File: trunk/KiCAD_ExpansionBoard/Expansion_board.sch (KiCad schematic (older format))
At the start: 2 parts

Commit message: Creation of project (sheets) structure and add some library schematic component (transceiver.lib, headers, etc.)
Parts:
- removed IC?: PIC16F876P, microchip-DIL28-6, symbol PIC16F876P
- removed P?: CONN_11, symbol CONN_11
- added U?: SN65HVD11, MODULE, symbol SN65HVD11
- added U?: SN65HVD234, MODULE, symbol SN65HVD234
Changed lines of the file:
@@
 EESchema Schematic File Version 2
+LIBS:boosterpack
 LIBS:power
 LIBS:device
@@
 LIBS:contrib
 LIBS:valves
+LIBS:transceiver
 LIBS:TM4C123G_CommExpBoard-cache
 EELAYER 27 0
@@
 Date "9 jun 2014"
 Rev "0.1"
-Comp "Luca Buccolini, student @ Università Politecnica delle Marche"
+Comp "Luca Buccolini, Student @ Università Politecnica delle Marche"
 Comment1 "Expansion Board for the Texas Instruments TM4C123G Launchpad "
 Comment2 ""
@@
 $EndDescr
 $Comp
-L PIC16F876P IC?
-U 1 1 5395B88F
-P 5150 2650
-F 0 "IC?" H 4450 3600 50  0000 L BNN
-F 1 "PIC16F876P" H 5450 1650 50  0000 L BNN
-F 2 "microchip-DIL28-6" H 5150 2800 50  0001 C CNN
-F 3 "" H 5150 2650 60  0000 C CNN
-	1    5150 2650
+L SN65HVD11 U?
+U 1 1 5395F741
+P 5350 2200
+F 0 "U?" H 5350 2100 50  0000 C CNN
+F 1 "SN65HVD11" H 5350 2300 50  0000 C CNN
+F 2 "MODULE" H 5350 2200 50  0001 C CNN
+F 3 "http://www.farnell.com/datasheets/1808277.pdf" H 5350 2200 50  0001 C CNN
+F 4 "Farnell" H 5350 2200 50  0001 C CNN "Supplier 1"
+F 5 "1100955" H 5350 2200 50  0001 C CNN "Supplier 1 P/N"
+F 6 "SN65HVD11D" H 5350 2200 50  0001 C CNN "Producer P/N"
+	1    5350 2200
 	1    0    0    -1
 $EndComp
 $Comp
-L CONN_11 P?
-U 1 1 5395B89E
-P 8250 3350
-F 0 "P?" V 8200 3350 60  0000 C CNN
-F 1 "CONN_11" V 8300 3350 60  0000 C CNN
-F 2 "" H 8250 3350 60  0000 C CNN
-F 3 "" H 8250 3350 60  0000 C CNN
-	1    8250 3350
+L SN65HVD234 U?
+U 1 1 5395F75E
+P 8250 2250
+F 0 "U?" H 8250 2150 50  0000 C CNN
+F 1 "SN65HVD234" H 8250 2350 50  0000 C CNN
+F 2 "MODULE" H 8250 2250 50  0001 C CNN
+F 3 "http://www.farnell.com/datasheets/1808424.pdf" H 8250 2250 50  0001 C CNN
+F 4 "Farnell" H 8250 2250 50  0001 C CNN "Supplier 1"
+F 5 "1212363" H 8250 2250 50  0001 C CNN "Supplier 1 P/N"
+F 6 "SN65HVD234D" H 8250 2250 50  0001 C CNN "Producer P/N"
+	1    8250 2250
 	1    0    0    -1
 $EndComp

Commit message: Circuit board schematic complete! TODO: Update schematic according new received specifics: "note-expansionboard_20140623.txt"
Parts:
- added C1: 10u, ~, symbol C
- added C2, C4: 100n, ~, symbol C
- added C3: 22u, ~, symbol C
- added D1: LED_R, SM_0603_MD, symbol LED
- added L1: 2u2, ~, symbol INDUCTOR_SMALL
- added P5: ANT, ~, symbol TST
- added Q1: NTR4101P, ~, symbol MOS_P
- added R1, R10, R11, R16, R17: 0, ~, symbol R
- added R12: 750, ~, symbol R
- added R13, R15: 560, ~, symbol R
- added R14, R4: 120, ~, symbol R
- added R18, R2, R7, R8, R9: 10k, ~, symbol R
- added R3: 100k, ~, symbol R
- added R5: 300k, ~, symbol R
- added R6: 95k3, ~, symbol R
- added SW? (x3): DIP_SWITCH, ~, symbol DIP_SWITCH
- added SW?: DIP_SWITCH_X1, ~, symbol DIP_SWITCH_X1
- added TVS1, TVS2: CDSOT23-SM712, ~, symbol CDSOT23-SM712
- added U2: TPS62160, MODULE, symbol TPS62160
- added U4: RFM23B, symbol RFM23B
- U1: renamed from U?; Descriprion (none) -> TRANSCEIVER CAN, 65HVD234, SOIC8; Producer (none) -> Texas Instruments
- U3: renamed from U?; Descriprion (none) -> 3.3-V RS-485 TRANSCEIVERS; Producer (none) -> Texas Instruments
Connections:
- net labels added: +12V_BUS, +3.3V_EB, +3.3V_TLP, +5V_TLP, CAN0_EN, CAN0_RS, CAN0_RX, CAN0_TX, CAN_H, CAN_L, GND, RFM_CLK, RFM_GPIO0, RFM_GPIO1, RFM_MISO, RFM_MOSI, RFM_NIRQ, RFM_SCLK, RFM_SDN, RFM_SSEL, RS485_A, RS485_B, RS485_RXEN#, RS485_TXEN, UART3_RX, UART3_TX
- wire segments 0 -> 126
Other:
- note added: "CAN transceiver"
- note added: "Power supply\n"
- note added: "RF module"
- note added: "RS-485 transceiver"
- note added: "Resistor on CAN0_RS line is \nfor slope control (optional)"
- note added: "mount R 10 ohm in place \nof R 0 ohm to improve \nsurge/ESD/EFT protection"
- moved on the sheet: U1, U3

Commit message: -Unito le due linee a 3.3V e riposizionato Q1 che ora va ad interrompere la linea di alimentazione a 3.3V dello switching quando è presente la +5V_TLP (USB). In serie al gate ho messo R8 da 120 ohm e ho lasciato R7 da 10k di pull-down.
-Ho messo un NPN, Q3, che ha al suo interno un partitore da 22k + 47k; è pilotato dalla +5V_TLP ed ho messo R1 verso +12V_BUS che mantiene attivo lo switching a meno che non sia presente la +5V_TLP (Q3 ON). Infine ho posizionato il led a monte del PMOS.

-Per la protezione dalle sovratensioni sulla +5V_TLP ho inserito, all'ingesso, TVS4 che è bidirezionale con tensione di lavoro a 5V e tensione di breakdown di 5.8V (min).

-Rimosse tutte le resistenze di pull-up nei transceiver: ne avevano alcune già internamente.

-Sostituiti gli header-jumper per i terminatori e la rete di fail-safe biasing con un SPDT (SW1), ed un 4PDT (SW2).

In serie al pin RS del transceiver ho messo una 10k.

Pull-up da 10k su SDN dell'RF module
 
Ho inserito un secondo TP P1, ANT_GND che posizionerò vicino al primo, P5, ANT_C per il collegamento dell'antenna.

-MISURA DELLA TENSIONE DI BUS: V_AN_MONITOR: ho ricalcolato i valori di R19 e R20 per ottenere un divider ratio pari a 6.236 circa anziché 6.206 come indicato. La tensione di fondo scala sarà vicina ai 20 V.

-Il TVS3 (SMCJ12CA) indicato è bidirezionale (DS: http://www.farnell.com/datasheets/1794554.pdf), così ho corretto il simbolo mettendone uno appropriato.

-Sostituito lo "spare-function header" da 2x4 pin con uno 2x5 pin reimpostando pin-out come indicato, comprensivo di massa ed alimentazione.
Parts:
- removed R9: 10k, ~, symbol R
- removed SW? (x3): DIP_SWITCH, ~, symbol DIP_SWITCH
- removed SW?: DIP_SWITCH_X1, ~, symbol DIP_SWITCH_X1
- added P1: ANT_GND, ~, symbol TST
- added Q3: PDTC124XT, SOT23_MD, symbol NPN_DIGITAL
- added SW1: SLIDE_SWITCH_SPDT, ~, symbol SLIDE_SWITCH_SPDT
- added SW2: SLIDE_SWITCH_4PDT, ~, symbol SLIDE_SWITCH_4PDT
- P5: value ANT -> ANT_C
- R1: value 0 -> 10k; Descriprion RESISTORE, 0805, 0R, ANTI SOLFATAZIONE -> RESISTOR, 0805, 10K, 1%, ANTI SULFUR; Producer P/N MCMR08X000 PTL -> MCMR08X1002FTL; Supplier 1 P/N 2073603 -> 2073607
- R8: value 10k -> 120; Descriprion RESISTOR, 0805, 10K, 1%, ANTI SULFUR -> RESISTOR, 0805, 120R, 1%, ANTI SULFUR; Producer P/N MCMR08X1002FTL -> MCMR08X1200FTL; Supplier 1 P/N 2073607 -> 2073624
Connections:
- net labels added: +3.3V
- net labels removed: +3.3V_EB, +3.3V_TLP
- wire segments 126 -> 128
- no-connect marks 0 -> 4
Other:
- note removed: "Resistor on CAN0_RS line is \nfor slope control (optional)"
- moved on the sheet: C1, C2, C3, C4, D1, L1, P5, Q1, R10, R11, R12, R13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

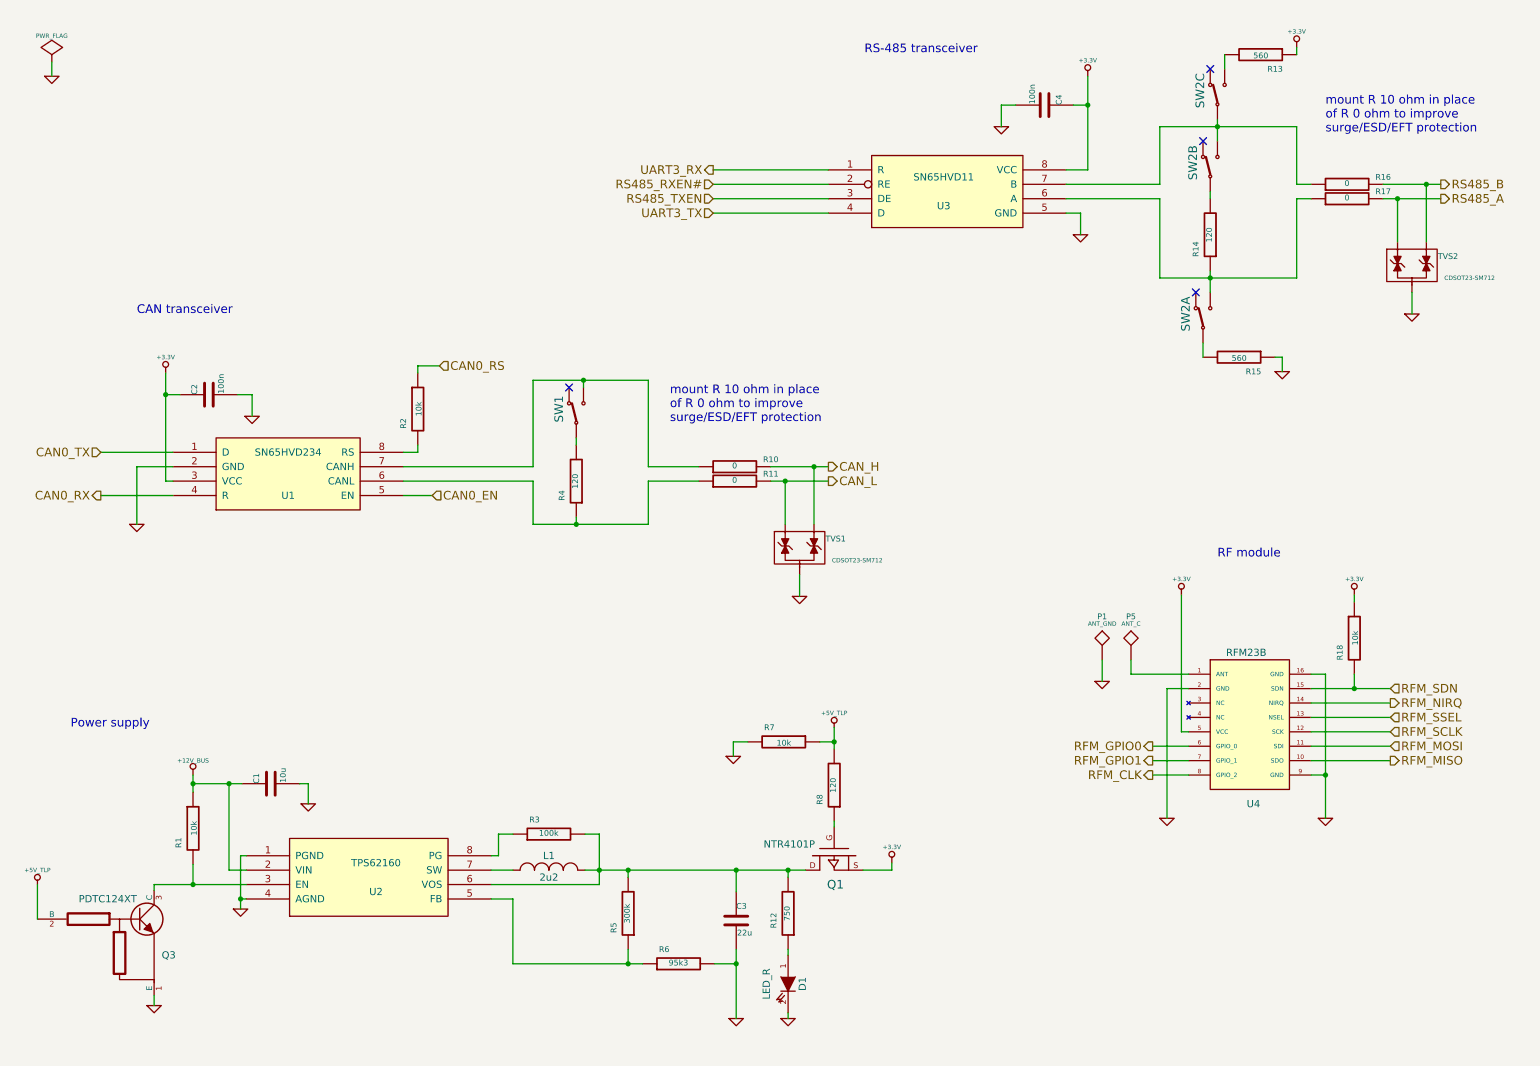
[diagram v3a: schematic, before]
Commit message: -Eliminata R7> con l-aggiunta di Q3 ora il pull down [ incorporato in esso, un-altro sprecher' solo corrente -Aumentate R1 e R18 a 100k -Modificata la connessione di SW2 per minimizzare la capacit' sul bus
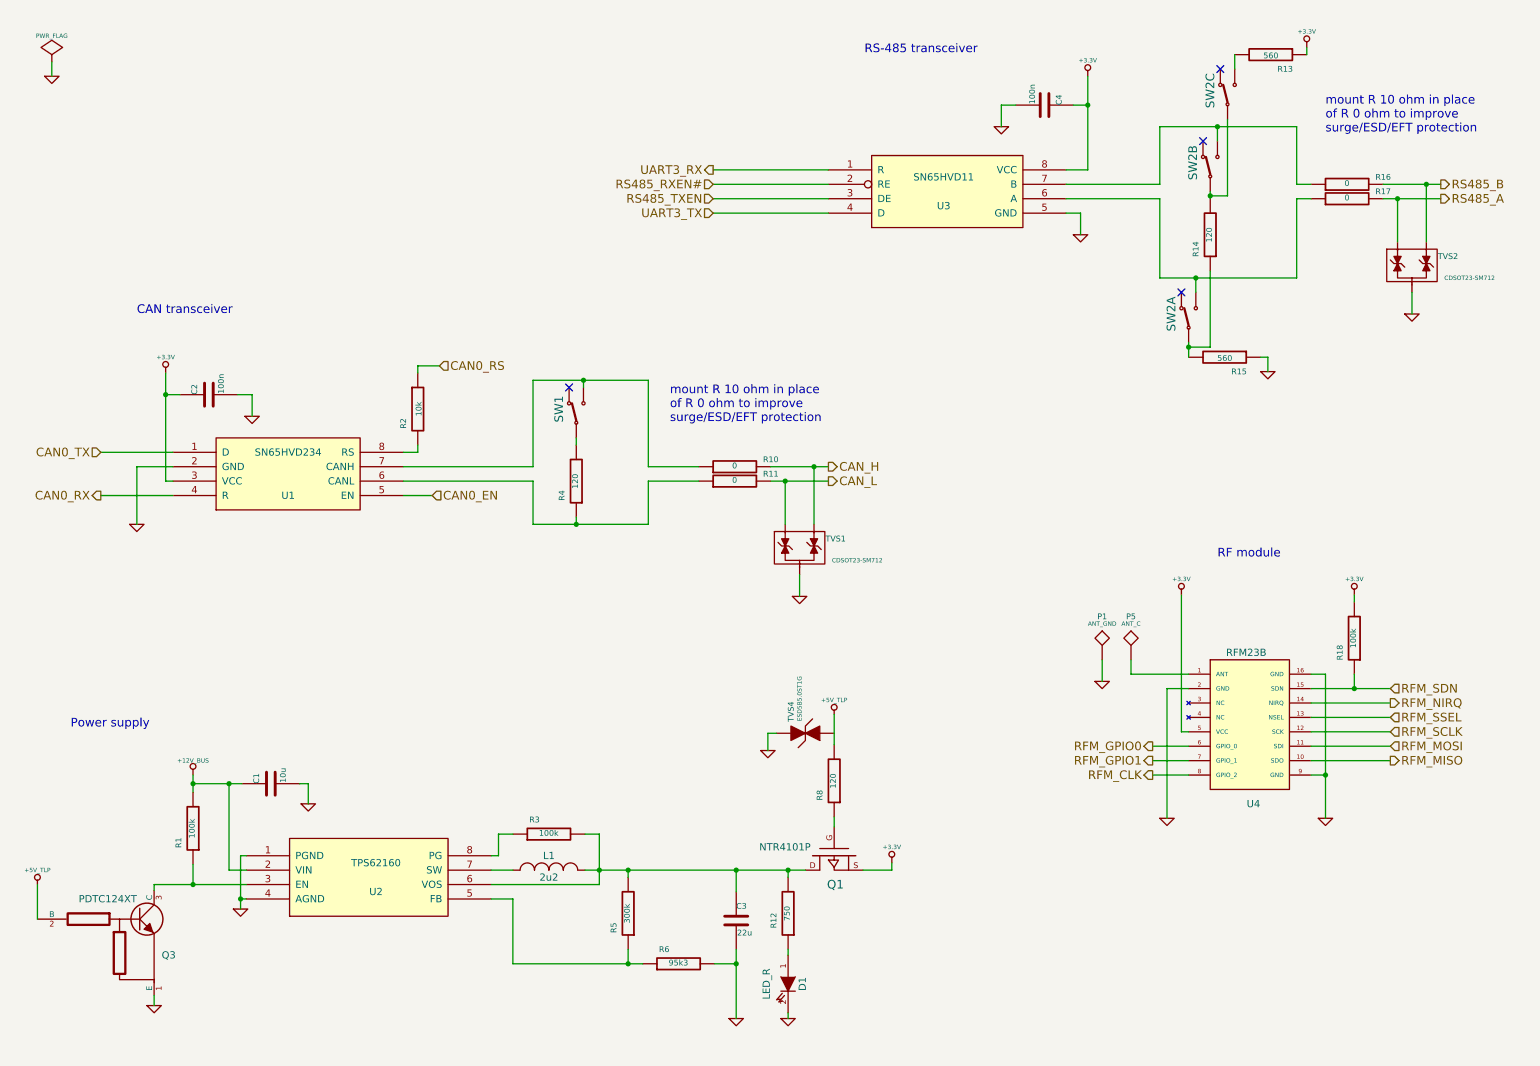
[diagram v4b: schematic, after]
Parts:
- removed R7: 10k, ~, symbol R
- added TVS4: ESD5B5.0ST1G, SOD-523_MD, symbol BID_TVS
- R1, R18: value 10k -> 100k; Descriprion RESISTOR, 0805, 10K, 1%, ANTI SULFUR -> RESISTOR, 0805, 100K, 1%, THICK FILM CHIP RESISTOR; Producer MULTICOMP -> VISHAY DRALORIC; Producer P/N MCMR08X1002FTL -> CRCW0805100KFKTA; Supplier 1 P/N 2073607 -> 1652905
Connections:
- net +12V_BUS: now also R1.2; no longer R1.1
- net +3.3V: now also R18.2; no longer R18.1
- net GND: now also TVS4.1
- net RFM_SDN: now also R18.1; no longer R18.2
- net at R17.1, SW2.3 (P2), U3.6 (A): no longer R14.1
- net at R16.1, SW2.6 (P2), U3.7 (B): no longer SW2.8 (COM)
- net at Q3.3 (C), U2.3 (EN): now also R1.1; no longer R1.2
- net at R14.2, SW2.5 (COM): now also SW2.8 (COM)
- net at R15.2, SW2.2 (COM): now also R14.1
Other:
- moved on the sheet: R13, R15, R8, SW2A, SW2C

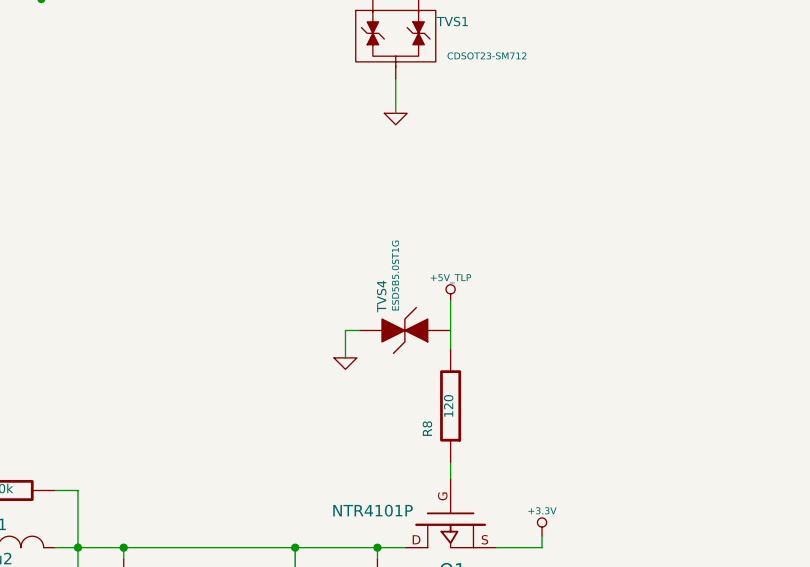
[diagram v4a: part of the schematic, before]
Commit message: -Aggiunta R7 in serie a monte del TVS4. Se non occorre, sostituire con una 0ohm.
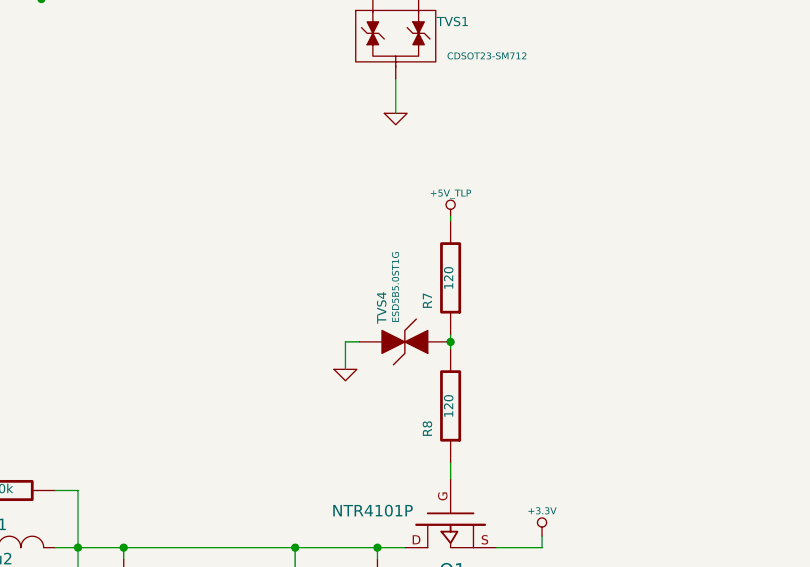
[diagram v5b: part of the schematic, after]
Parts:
- added R7: 120, ~, symbol R
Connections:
- net +5V_TLP: now also R7.2; no longer R8.2
- net at TVS4.2: now also R8.2, R7.1
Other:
- moved on the sheet: TVS4
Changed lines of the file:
@@
 Sheet 2 3
 Title "TM4C123G Communication Expansion Board"
-Date "11 jul 2014"
-Rev "0.3"
+Date "15 jul 2014"
+Rev "0.3.1"
 Comp "Luca Buccolini, Student @ Università Politecnica delle Marche"
 Comment1 "Expansion Board for the Texas Instruments TM4C123G Launchpad "
@@
 L +5V_TLP #PWR06
 U 1 1 5399C6C9
-P 6280 5340
-F 0 "#PWR06" H 6280 5430 20  0001 C CNN
-F 1 "+5V_TLP" H 6280 5440 30  0000 C CNN
-F 2 "" H 6280 5340 60  0000 C CNN
-F 3 "" H 6280 5340 60  0000 C CNN
-	1    6280 5340
+P 6280 4970
+F 0 "#PWR06" H 6280 5060 20  0001 C CNN
+F 1 "+5V_TLP" H 6280 5070 30  0000 C CNN
+F 2 "" H 6280 4970 60  0000 C CNN
+F 3 "" H 6280 4970 60  0000 C CNN
+	1    6280 4970
 	1    0    0    -1
 $EndComp
@@
 	6280 6050 6280 6120
 Wire Wire Line
-	6280 5340 6280 5550
-Wire Wire Line
 	6680 6370 6680 6420
 Wire Wire Line
@@
 L GND #PWR027
 U 1 1 53BFC020
-P 5820 5590
-F 0 "#PWR027" H 5820 5590 30  0001 C CNN
-F 1 "GND" H 5820 5520 30  0001 C CNN
-F 2 "" H 5820 5590 60  0000 C CNN
-F 3 "" H 5820 5590 60  0000 C CNN
-	1    5820 5590
+P 5820 5640
+F 0 "#PWR027" H 5820 5640 30  0001 C CNN
+F 1 "GND" H 5820 5570 30  0001 C CNN
+F 2 "" H 5820 5640 60  0000 C CNN
+F 3 "" H 5820 5640 60  0000 C CNN
+	1    5820 5640
 	1    0    0    -1
 $EndComp
@@
 L BID_TVS TVS4
 U 1 1 53BFC02B
-P 6080 5470
-F 0 "TVS4" H 6230 5570 40  0000 C CNN
-F 1 "ESD5B5.0ST1G" H 6320 5510 30  0000 C CNN
-F 2 "SOD-523_MD" V 5780 5470 60  0001 C CNN
-F 3 "http://www.onsemi.com/pub/Collateral/ESD5B5.0ST1G.PDF" H 6330 5520 60  0001 C CNN
-F 4 "Farnell" H 6080 5470 60  0001 C CNN "Supplier 1"
-F 5 "2317513" H 6080 5470 60  0001 C CNN "Supplier 1 P/N"
-F 6 "ON SEMICONDUCTOR" H 6080 5470 60  0001 C CNN "Producer"
-F 7 "ESD5B5.0ST1G" H 6080 5470 60  0001 C CNN "Producer P/N"
-F 8 "ESD PROTECTION DIODE, 5V, SOD-523-2" H 6080 5470 60  0001 C CNN "Descriprion"
-	1    6080 5470
+P 6080 5520
+F 0 "TVS4" H 6230 5620 40  0000 C CNN
+F 1 "ESD5B5.0ST1G" H 6320 5560 30  0000 C CNN
+F 2 "SOD-523_MD" V 5780 5520 60  0001 C CNN
+F 3 "http://www.onsemi.com/pub/Collateral/ESD5B5.0ST1G.PDF" H 6330 5570 60  0001 C CNN
+F 4 "Farnell" H 6080 5520 60  0001 C CNN "Supplier 1"
+F 5 "2317513" H 6080 5520 60  0001 C CNN "Supplier 1 P/N"
+F 6 "ON SEMICONDUCTOR" H 6080 5520 60  0001 C CNN "Producer"
+F 7 "ESD5B5.0ST1G" H 6080 5520 60  0001 C CNN "Producer P/N"
+F 8 "ESD PROTECTION DIODE, 5V, SOD-523-2" H 6080 5520 60  0001 C CNN "Descriprion"
+	1    6080 5520
 	0    -1   -1   0
 $EndComp
 Wire Wire Line
-	5820 5590 5820 5470
-Wire Wire Line
-	5820 5470 5880 5470
+	5820 5640 5820 5520
+Wire Wire Line
+	5820 5520 5880 5520
+$Comp
+L R R7
+U 1 1 53C521B1
+P 6280 5240
+F 0 "R7" V 6380 5340 40  0000 C CNN
+F 1 "120" V 6287 5241 40  0000 C CNN
+F 2 "~" V 6210 5240 30  0000 C CNN
+F 3 "http://www.farnell.com/datasheets/1716708.pdf" H 6280 5240 30  0001 C CNN
+F 4 "Farnell" H 6280 5240 60  0001 C CNN "Supplier 1"
+F 5 "2073624" H 6280 5240 60  0001 C CNN "Supplier 1 P/N"
+F 6 "MULTICOMP" H 6280 5240 60  0001 C CNN "Producer"
+F 7 "MCMR08X1200FTL" H 6280 5240 60  0001 C CNN "Producer P/N"
+F 8 "RESISTOR, 0805, 120R, 1%, ANTI SULFUR" H 6280 5240 60  0001 C CNN "Descriprion"
+	1    6280 5240
+	-1   0    0    1
+$EndComp
+Wire Wire Line
+	6280 4970 6280 4990
+Wire Wire Line
+	6280 5490 6280 5550
+Connection ~ 6280 5520
 $EndSCHEMATC
